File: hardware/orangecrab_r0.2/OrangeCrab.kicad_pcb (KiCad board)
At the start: 6 copper layers, 50.8 x 22.9 mm, 157 parts, among them J1 Conn_01x12_Male, J2 Conn_01x16_Male, J3 USB_B_Micro, J4 MicroSd, J5 JST, J6 JTAG, SW1 SW_Push, U1 FAN53541, U10 NCP115-2.5, U2 FAN53541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

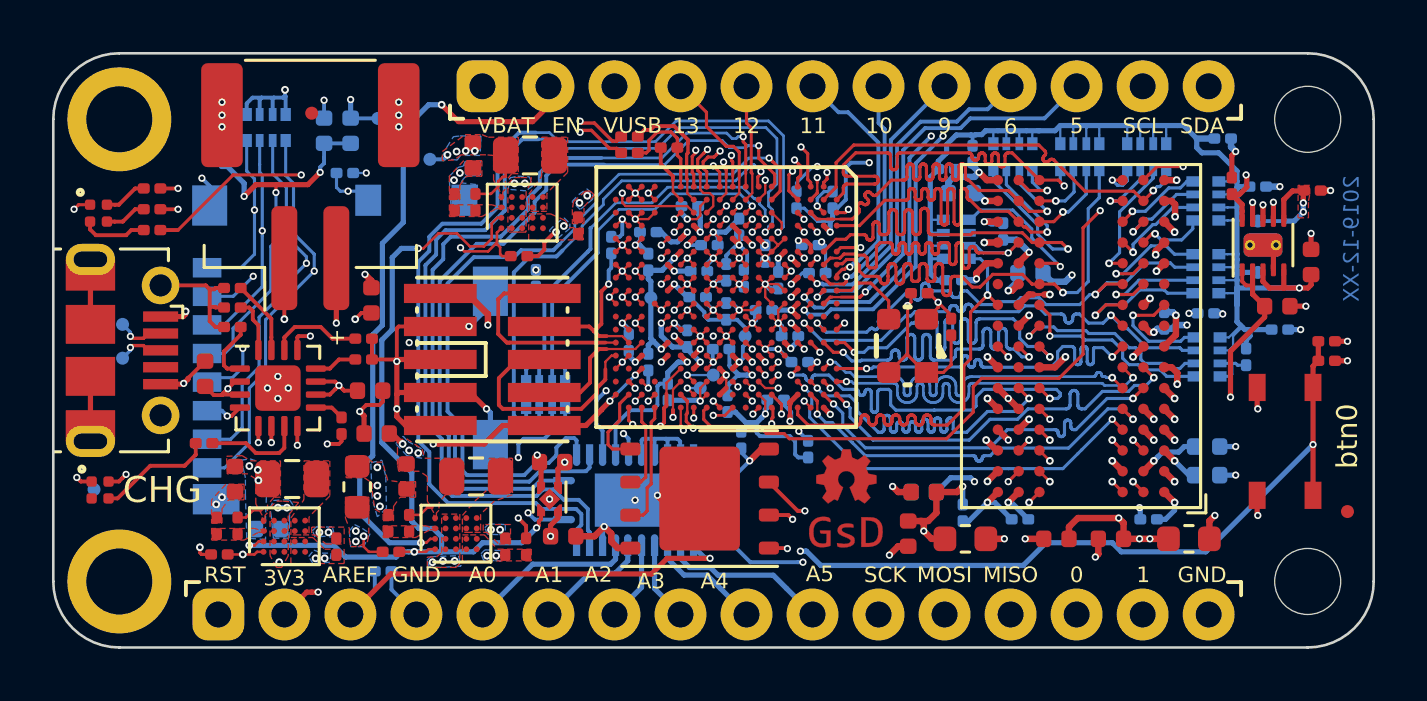
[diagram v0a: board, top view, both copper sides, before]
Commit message: hw: Route last FPGA I/O to A[0-5]
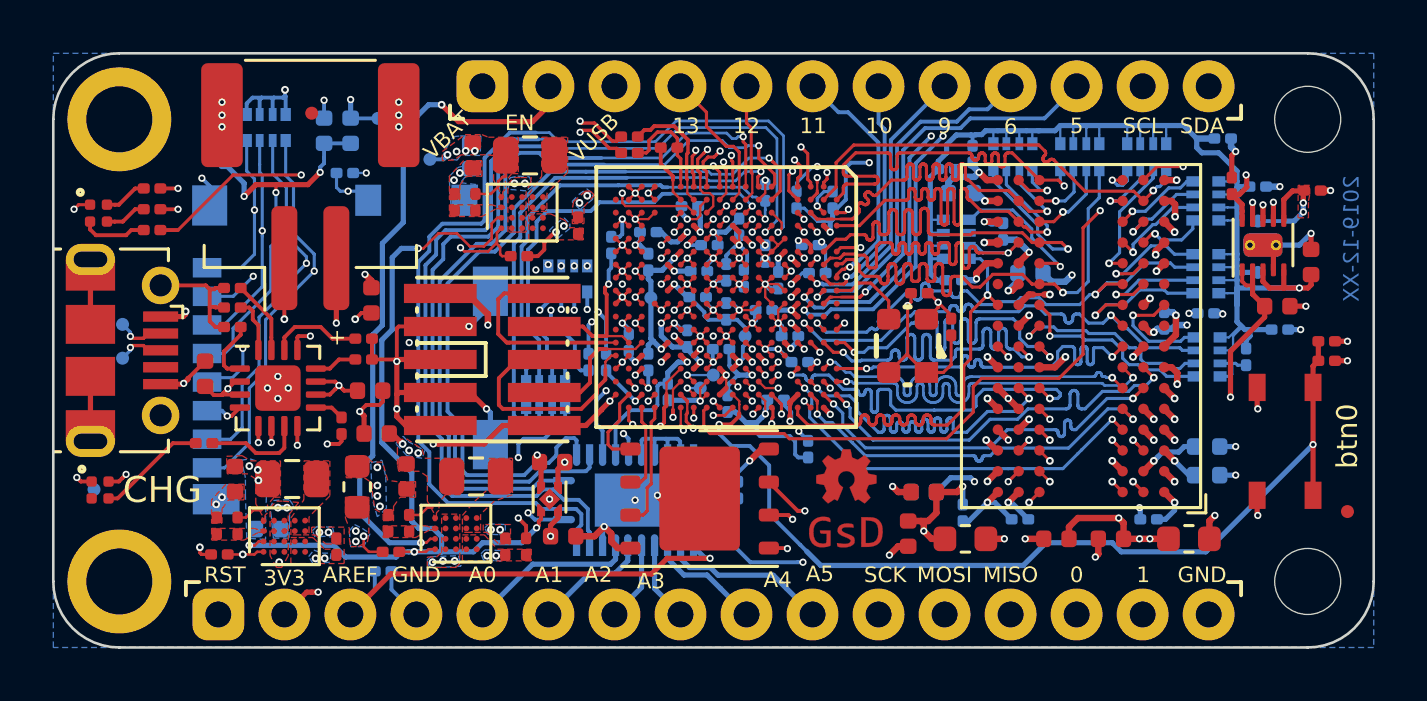
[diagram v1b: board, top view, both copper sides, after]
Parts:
- added R3: 20R, Resistor_SMD:R_0201_0603Metric, B.Cu at (155.8, 103.4)
- added R6: 20R, Resistor_SMD:R_0201_0603Metric, B.Cu at (155.1, 103.4)
- added RN10: 10k, Resistor_SMD:R_Array_Convex_4x0402, B.Cu at (154.3, 100.2)
- moved C28 9.42 mm to (161.9, 96.9)
- moved C69 1.93 mm to (160.9, 108.3), turned to 270 degrees
- moved C16 0.10 mm to (150.6, 95.5)
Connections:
- U3 pad G4: Net-(U3-PadG4) -> IO_A4
- U3 pad H4: Net-(U3-PadH4) -> IO_A3
- U3 pad J17: Net-(U3-PadJ17) -> USER_BUTTON
- U3 pad L4: Net-(U3-PadL4) -> IO_A0
- U3 pad N3: Net-(U3-PadN3) -> IO_A1
- U3 pad N4: Net-(U3-PadN4) -> IO_A2
- U3 pad T17: USER_BUTTON -> IO_A5
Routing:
- net /sheetIO/A5: track 6.42 -> 29.7 mm, vias 0 -> 1
- net /sheetIO/A4: track 4.38 -> 25.2 mm, vias 0 -> 1
- net /sheetIO/A3: track 3.02 -> 21.7 mm, vias 0 -> 1
- net /sheetIO/A2: track 3.04 -> 20.7 mm, vias 0 -> 1
- net /sheetIO/A1: track 4.44 -> 20.4 mm, vias 0 -> 1
- net /sheetIO/A0: track 6.48 -> 21.3 mm, vias 0 -> 1
- net IO_A4: track 0.00 -> 14.2 mm, vias 0 -> 2
- net Net-(U3-PadH4): track 10.3 -> 0.00 mm, vias 1 -> 0
- net Net-(U3-PadG4): track 10.2 -> 0.00 mm, vias 1 -> 0
- net IO_A3: track 0.00 -> 10.2 mm, vias 0 -> 2
- net Net-(U3-PadL4): track 9.13 -> 0.00 mm, vias 1 -> 0
- net IO_A0: track 0.00 -> 8.07 mm, vias 0 -> 2
- net GND: track 203.9 -> 209.7 mm
- net IO_A1: track 0.00 -> 5.67 mm, vias 0 -> 2
- net IO_A2: track 0.00 -> 5.08 mm, vias 0 -> 2
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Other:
- board text removed: "Micro SD"

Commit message: hw: Update fiducials Add pullup to FLASH CS/SCK line Update BOM part numbers Fix Button pull-up voltage
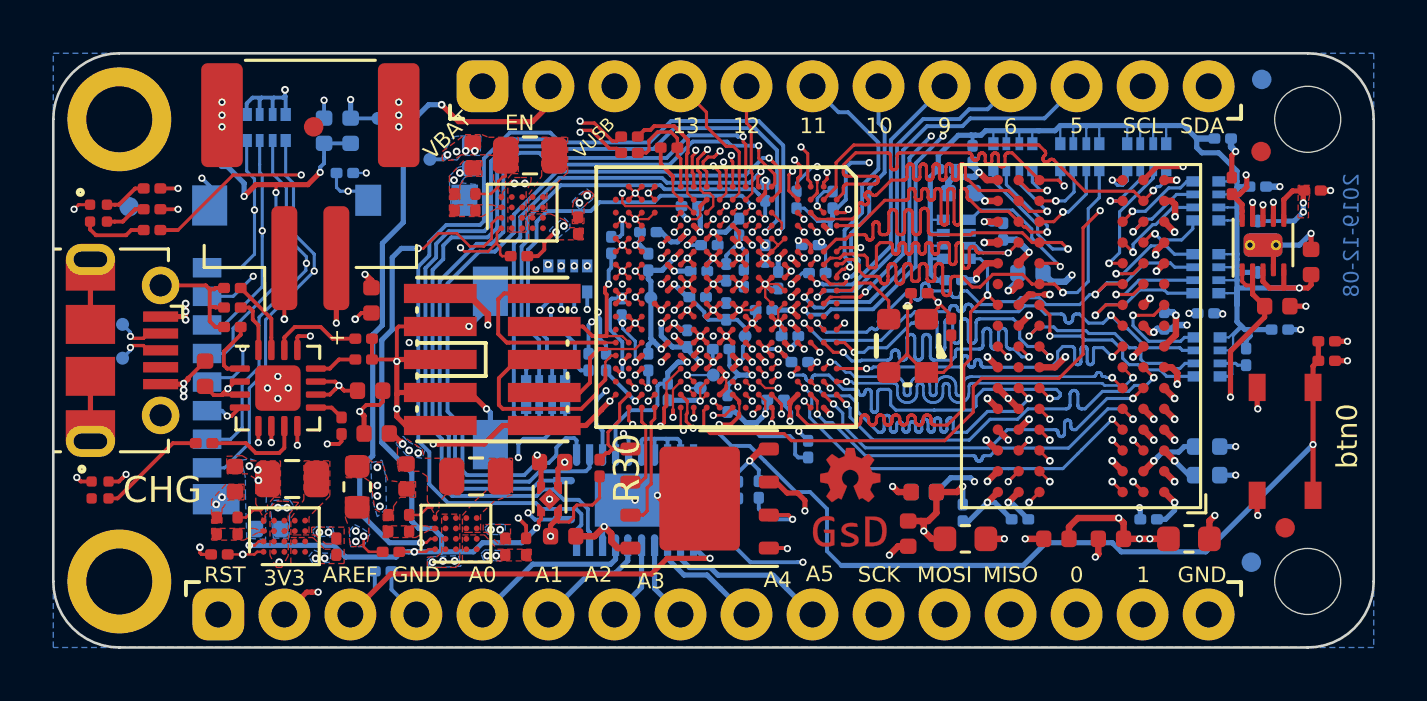
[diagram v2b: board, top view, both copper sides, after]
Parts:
- removed REF** (x3): Fiducial_0.5mm_Mask1mm, Fiducial:Fiducial_0.5mm_Mask1mm
- added FID1: Fiducial, Fiducial:Fiducial_0.75mm_Mask1.5mm, B.Cu at (137.4, 97.4)
- added FID2: Fiducial, Fiducial:Fiducial_0.75mm_Mask1.5mm, F.Cu at (144.5, 94.3)
- added FID3: Fiducial, Fiducial:Fiducial_0.75mm_Mask1.5mm, B.Cu at (181.0, 92.5)
- added FID4: Fiducial, Fiducial:Fiducial_0.75mm_Mask1.5mm, F.Cu at (181.9, 109.8)
- added FID5: Fiducial, Fiducial:Fiducial_0.75mm_Mask1.5mm, B.Cu at (180.6, 111.1)
- added FID6: Fiducial, Fiducial:Fiducial_0.75mm_Mask1.5mm, F.Cu at (181.0, 95.3)
- added R30: 4.7K, Resistor_SMD:R_0201_0603Metric, F.Cu at (155.5, 107.5)
- added R31: 1K, Resistor_SMD:R_0201_0603Metric, B.Cu at (161.7, 108.3)
- C28: value C -> 100nF
- R3, R6: value 20R -> 50R
- RN10: value 10k -> 50R
- RN9: value 10k -> 10K
- U6: value AT25SF081 -> W25Q128JVP
- U9: value CD74HC4067M -> 74HC4067BQ
- moved C67 1.40 mm to (156.4, 101.3)
- moved G*** 0.16 mm to (165.2, 107.8)
- moved G*** 0.15 mm to (165.2, 110.0)
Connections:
- R4 pad 1: P3.3V -> P1.35V
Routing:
- net GND: track 209.7 -> 232.6 mm, vias 143 -> 145
- net P1.35V: track 89.8 -> 96.3 mm, vias 17 -> 18
- net P3.3V: track 62.9 -> 68.0 mm
- net SPI_CONFIG_SCK: track 11.2 -> 13.1 mm
- net ECP5_VREF: track 60.8 -> 59.4 mm
- net SPI_CONFIG_SS: track 3.19 -> 3.85 mm
- net PUSB_VBUS: track 29.9 -> 30.6 mm, vias 3 -> 5
- net IO_A4: track 14.2 -> 13.7 mm
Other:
- net class DDR3_CTRL_LM1.0: clearance 0.1016 -> 0.0889
- board text added: "2019-12-08"
- board text removed: "2019-12-XX"
